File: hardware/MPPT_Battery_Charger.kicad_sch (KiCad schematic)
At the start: 74 parts, among them Q24 SI7414DN-T1-E3, Q25 SI7414DN-T1-E3, Q5 SI2302DDS-T1-GE3, Q5 SI7414DN-T1-E3, Q6 SI7414DN-T1-E3, U22 BQ24650RVAT, U26 LMV321RIYLT, U28 LMV321RIYLT, U4 INA199C1DCKR

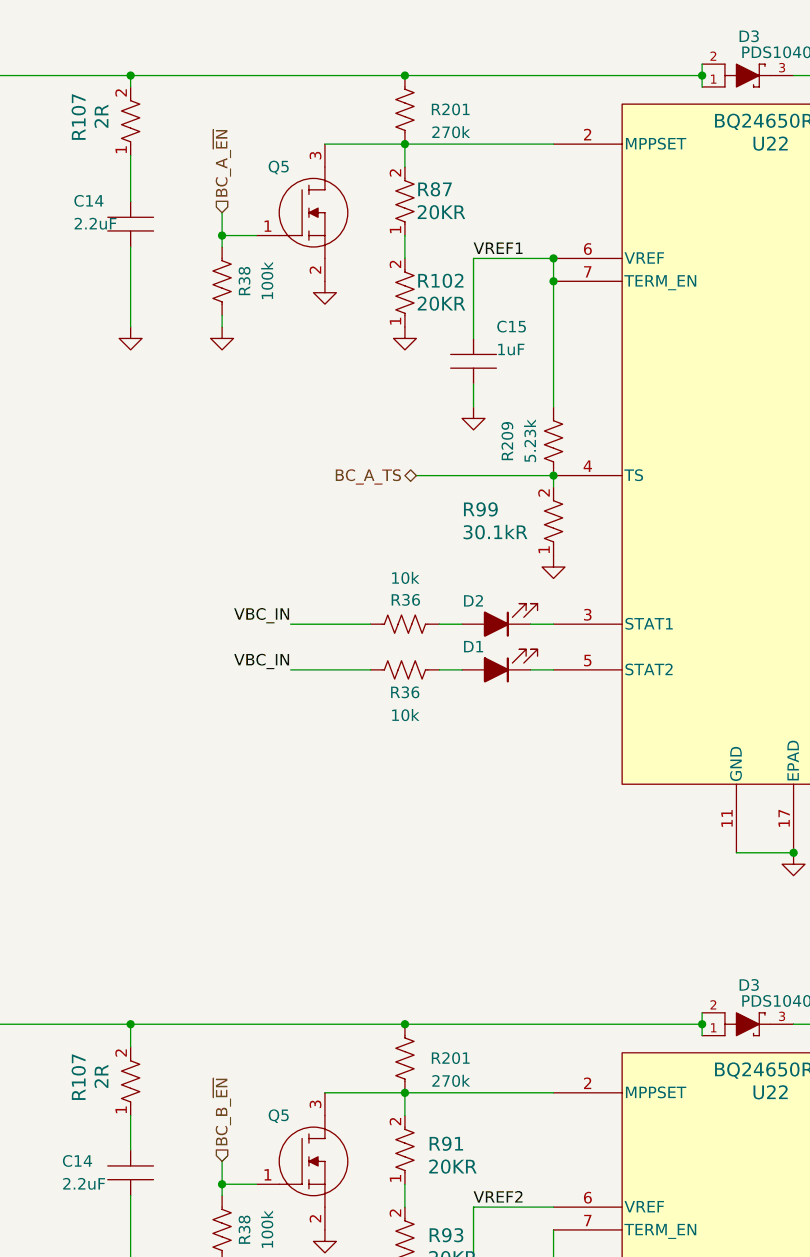
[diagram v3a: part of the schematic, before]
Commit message: hardware: All resistors added.
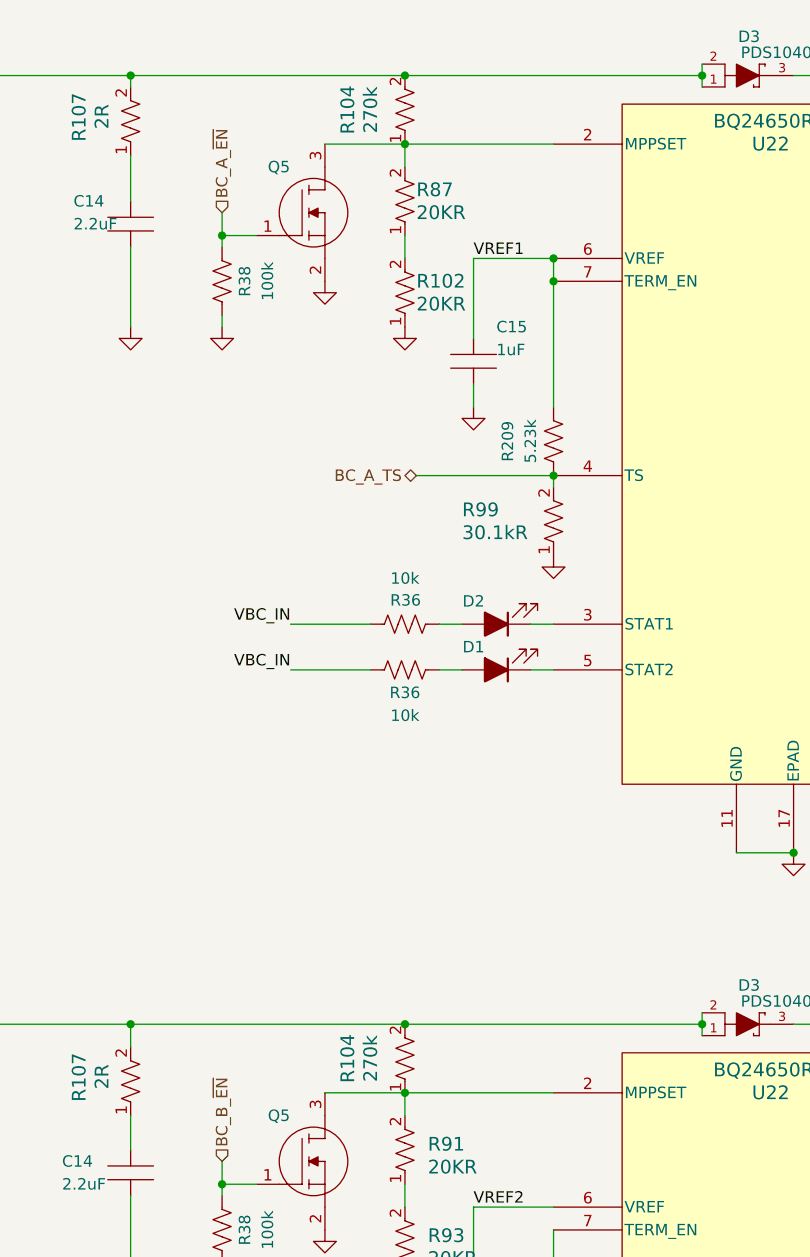
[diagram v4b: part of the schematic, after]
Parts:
- removed R201 (x2): 270k, symbol Device:R_US
- added R104 (x2): 270k, RES_CRCW_0805_VIS, symbol CRCW0805270KFKEAHP:CRCW080520K0FKEAHP
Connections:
- net VBC_N: now also R104.2, R104.2
- net at Q5.3 (D), R87.2, U22.2 (MPPSET): now also R104.1
- net at Q5.3 (D), R91.2, U22.2 (MPPSET): now also R104.1
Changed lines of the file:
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@@
   (junction (at 312.42 60.96) (diameter 0) (color 0 0 0 0)
   )
+  (junction (at 133.35 24.13) (diameter 0) (color 0 0 0 0)
+  )
   (junction (at 113.03 147.32) (diameter 0) (color 0 0 0 0)
   )
@@
   (junction (at 26.67 34.29) (diameter 0) (color 0 0 0 0)
   )
-  (junction (at 133.35 24.13) (diameter 0) (color 0 0 0 0)
-  )
   (junction (at 196.85 31.75) (diameter 0) (color 0 0 0 0)
   )
-  (junction (at 133.35 129.54) (diameter 0) (color 0 0 0 0)
-  )
   (junction (at 262.89 24.13) (diameter 0) (color 0 0 0 0)
   )
@@
   (junction (at 360.68 74.93) (diameter 0) (color 0 0 0 0)
   )
+  (junction (at 133.35 129.54) (diameter 0) (color 0 0 0 0)
+  )
   (junction (at 256.54 165.1) (diameter 0) (color 0 0 0 0)
   )
@@
     (stroke (width 0) (type default))
   )
-  (wire (pts (xy 133.35 129.54) (xy 166.37 129.54))
+  (wire (pts (xy 102.87 129.54) (xy 133.35 129.54))
     (stroke (width 0) (type default))
   )
@@
     (stroke (width 0) (type default))
   )
-  (wire (pts (xy 102.87 129.54) (xy 133.35 129.54))
-    (stroke (width 0) (type default))
-  )
   (wire (pts (xy 149.86 152.4) (xy 149.86 166.37))
     (stroke (width 0) (type default))
@@
     (stroke (width 0) (type default))
   )
-  (wire (pts (xy 133.35 24.13) (xy 166.37 24.13))
-    (stroke (width 0) (type default))
-  )
   (wire (pts (xy 223.52 50.8) (xy 226.06 50.8))
     (stroke (width 0) (type default))
@@
     (stroke (width 0) (type default))
   )
+  (wire (pts (xy 133.35 129.54) (xy 166.37 129.54))
+    (stroke (width 0) (type default))
+  )
   (wire (pts (xy 360.68 43.18) (xy 370.84 43.18))
     (stroke (width 0) (type default))
@@
     (stroke (width 0) (type default))
   )
+  (wire (pts (xy 133.35 24.13) (xy 166.37 24.13))
+    (stroke (width 0) (type default))
+  )
   (wire (pts (xy 196.85 60.96) (xy 196.85 63.5))
     (stroke (width 0) (type default))
@@
     )
   )
-  (symbol (lib_id "Device:R_US") (at 133.35 133.35 0) (unit 1)
+  (symbol (lib_id "CRCW0805270KFKEAHP:CRCW080520K0FKEAHP") (at 132.08 139.7 90) (unit 1)
     (in_bom yes) (on_board yes) (dnp no)
-    (property "Reference" "R201" (at 138.43 133.35 0)
-      (effects (font (size 1.27 1.27)))
+    (property "Reference" "R104" (at 127 133.35 0)
+      (effects (font (size 1.524 1.524)))
     )
-    (property "Value" "270k" (at 138.43 135.89 0)
-      (effects (font (size 1.27 1.27)))
+    (property "Value" "270k" (at 129.54 133.35 0)
+      (effects (font (size 1.524 1.524)))
     )
-    (property "Footprint" "" (at 134.366 133.604 90)
-      (effects (font (size 1.27 1.27)) hide)
+    (property "Footprint" "RES_CRCW_0805_VIS" (at 132.08 139.7 0)
+      (effects (font (size 1.27 1.27) italic) hide)
     )
-    (property "Datasheet" "~" (at 133.35 133.35 0)
-      (effects (font (size 1.27 1.27)) hide)
+    (property "Datasheet" "CRCW0805270KFKEAHP" (at 132.08 139.7 0)
+      (effects (font (size 1.27 1.27) italic) hide)
     )
     (pin "1")
@@
     (instances
       (project "eps-re_project"
-        (path "/2eebaa11-d7ed-4bfd-bc8e-988f68654d29/6f34948c-43a8-4614-b8ed-90c5b6b9b243"
-          (reference "R201") (unit 1)
+        (path "/2eebaa11-d7ed-4bfd-bc8e-988f68654d29/4f028e55-4c46-47b6-9c45-f6b50d9d4db8"
+          (reference "R104") (unit 1)
         )
         (path "/2eebaa11-d7ed-4bfd-bc8e-988f68654d29/0b69622c-4960-45c0-904b-657ff8db02ea"
@@
         )
       )
-      (project "EPSpg3"
-        (path "/95ab2aaf-8d7f-4e6e-818d-723704a56097"
-          (reference "R17") (unit 1)
-        )
-      )
     )
   )
@@
     )
   )
+  (symbol (lib_id "CRCW0805270KFKEAHP:CRCW080520K0FKEAHP") (at 132.08 34.29 90) (unit 1)
+    (in_bom yes) (on_board yes) (dnp no)
+    (property "Reference" "R104" (at 127 27.94 0)
+      (effects (font (size 1.524 1.524)))
+    )
+    (property "Value" "270k" (at 129.54 27.94 0)
+      (effects (font (size 1.524 1.524)))
+    )
+    (property "Footprint" "RES_CRCW_0805_VIS" (at 132.08 34.29 0)
+      (effects (font (size 1.27 1.27) italic) hide)
+    )
+    (property "Datasheet" "CRCW0805270KFKEAHP" (at 132.08 34.29 0)
+      (effects (font (size 1.27 1.27) italic) hide)
+    )
+    (pin "1")
+    (pin "2")
+    (instances
+      (project "eps-re_project"
+        (path "/2eebaa11-d7ed-4bfd-bc8e-988f68654d29/4f028e55-4c46-47b6-9c45-f6b50d9d4db8"
+          (reference "R104") (unit 1)
+        )
+        (path "/2eebaa11-d7ed-4bfd-bc8e-988f68654d29/0b69622c-4960-45c0-904b-657ff8db02ea"
+          (reference "R100") (unit 1)
+        )
+      )
+    )
+  )
   (symbol (lib_id "C1210C475K5RACTU:C1210C475K5RACTU") (at 270.51 64.77 0) (unit 1)
     (in_bom yes) (on_board yes) (dnp no)
@@
         )
       )
-    )
-  )
-  (symbol (lib_id "Device:R_US") (at 133.35 27.94 0) (unit 1)
-    (in_bom yes) (on_board yes) (dnp no)
-    (property "Reference" "R201" (at 138.43 27.94 0)
-      (effects (font (size 1.27 1.27)))
-    )
-    (property "Value" "270k" (at 138.43 30.48 0)
-      (effects (font (size 1.27 1.27)))
-    )
-    (property "Footprint" "" (at 134.366 28.194 90)
-      (effects (font (size 1.27 1.27)) hide)
-    )
-    (property "Datasheet" "~" (at 133.35 27.94 0)
-      (effects (font (size 1.27 1.27)) hide)
-    )
-    (pin "1")
-    (pin "2")
-    (instances
-      (project "eps-re_project"
-        (path "/2eebaa11-d7ed-4bfd-bc8e-988f68654d29/6f34948c-43a8-4614-b8ed-90c5b6b9b243"
-          (reference "R201") (unit 1)
-        )
-        (path "/2eebaa11-d7ed-4bfd-bc8e-988f68654d29/0b69622c-4960-45c0-904b-657ff8db02ea"
-          (reference "R100") (unit 1)
-        )
-      )
-      (project "EPSpg3"
-        (path "/95ab2aaf-8d7f-4e6e-818d-723704a56097"
-          (reference "R17") (unit 1)
-        )
-      )

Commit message: hardware: footprints
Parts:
- R104: footprint RES_CRCW_0805_VIS -> footprints:CRCW0805270KFKEAHP
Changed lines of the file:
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@@
   (symbol (lib_id "CRCW060330K0FKEAHP:RES") (at 52.07 226.06 90) (unit 1)
     (in_bom yes) (on_board yes) (dnp no)
-    (property "Reference" "R221" (at 46.99 219.71 0)
+    (property "Reference" "R221" (at 54.61 219.71 0)
       (effects (font (size 1.27 1.27)))
     )
-    (property "Value" "30k" (at 49.53 219.71 0)
+    (property "Value" "30k" (at 57.15 219.71 0)
       (effects (font (size 1.27 1.27)))
     )
@@
     )
   )
-  (symbol (lib_id "CRCW0805270KFKEAHP:CRCW080520K0FKEAHP") (at 132.08 34.29 90) (unit 1)
+  (symbol (lib_name "CRCW080520K0FKEAHP_1") (lib_id "CRCW0805270KFKEAHP:CRCW080520K0FKEAHP") (at 132.08 34.29 90) (unit 1)
     (in_bom yes) (on_board yes) (dnp no)
     (property "Reference" "R104" (at 127 27.94 0)
@@
       (effects (font (size 1.524 1.524)))
     )
-    (property "Footprint" "RES_CRCW_0805_VIS" (at 132.08 34.29 0)
+    (property "Footprint" "footprints:CRCW0805270KFKEAHP" (at 132.08 34.29 0)
       (effects (font (size 1.27 1.27) italic) hide)
     )
@@
     )
   )
-  (symbol (lib_id "CRCW20102R00FKEF:CRCW20102R00FKEF") (at 90.805 36.195 90) (unit 1)
+  (symbol (lib_name "CRCW20102R00FKEF_1") (lib_id "CRCW20102R00FKEF:CRCW20102R00FKEF") (at 90.805 36.195 90) (unit 1)
     (in_bom yes) (on_board yes) (dnp no) (fields_autoplaced)
     (property "Reference" "R107" (at 97.155 26.035 0)
